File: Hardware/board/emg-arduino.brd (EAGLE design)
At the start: 27.9 x 50.5 mm, 23 parts, among them U1 ATMEGA328P_TQFP, U2 LIS3DH, U3 TC1262, U4 BLUEFRUIT-LE

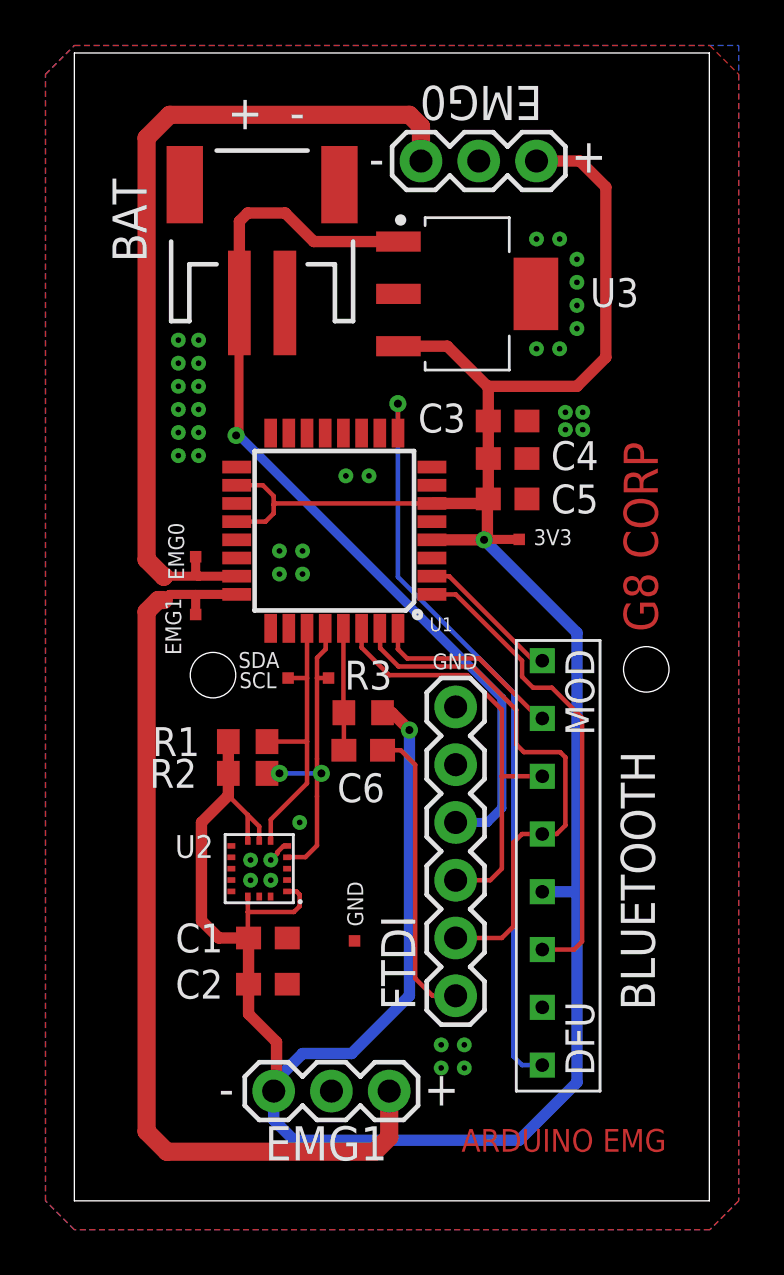
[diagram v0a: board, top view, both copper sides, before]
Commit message: changed bluetooth connector location
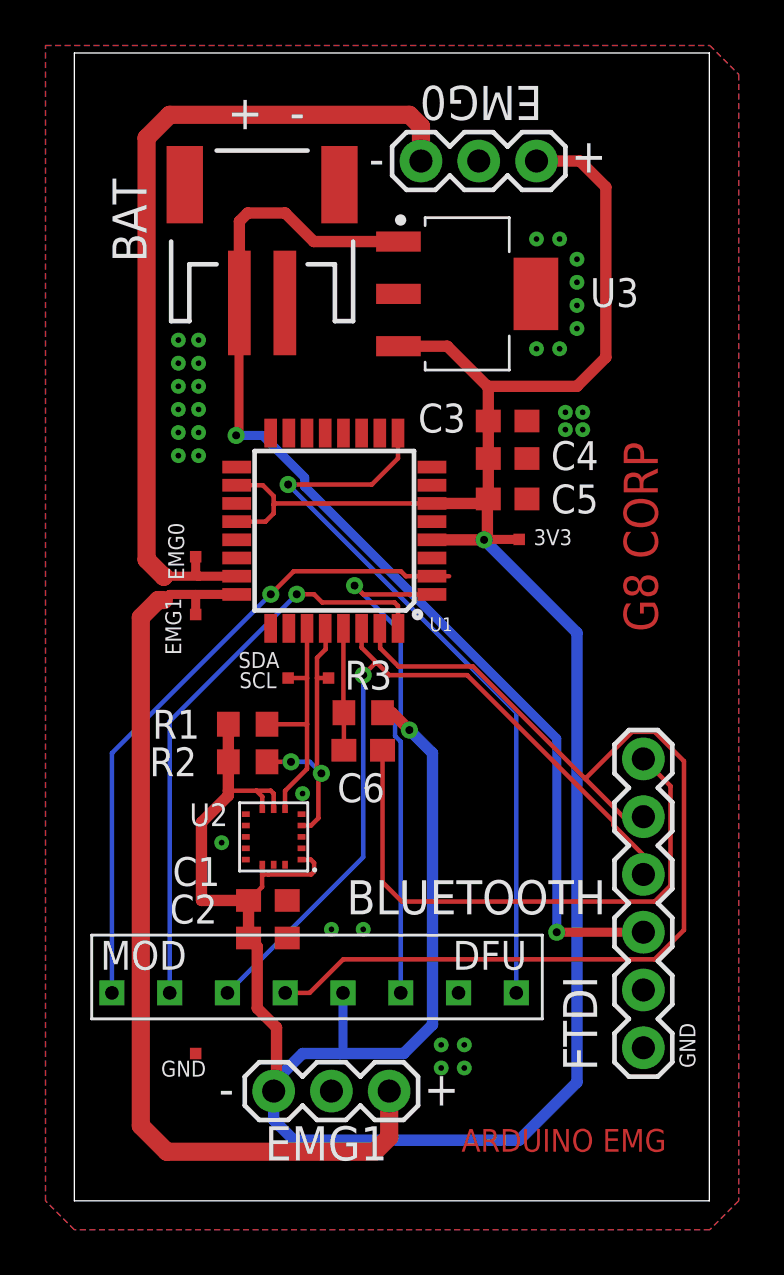
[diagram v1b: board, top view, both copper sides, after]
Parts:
- moved J1 13.3 mm to (25.0, 23.2), turned to 270 degrees
- moved U4 13.3 mm to (9.27, 13.0), turned to 0 degrees
- moved TP6 8.56 mm to (5.33, 10.3)
- moved C2 2.03 mm to (8.51, 15.4)
- moved C1 1.65 mm to (8.51, 17.0)
- moved U2 1.53 mm to (8.76, 19.8)
- moved R1 0.76 mm to (7.62, 24.8)
- moved R2 0.51 mm to (7.62, 23.1)
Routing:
- net AT_TXD: track 23.9 -> 47.4 mm
- net MOD: track 6.39 -> 28.8 mm, vias 0 -> 1
- net CTS: track 8.53 -> 25.8 mm, vias 0 -> 1
- net AT_RXD: track 19.1 -> 35.2 mm, vias 0 -> 1
- net N$6: track 13.2 -> 25.2 mm
- net VBAT: track 40.7 -> 49.3 mm, vias 1 -> 2
- net +3V3: track 137.2 -> 142.1 mm
- net SDA: track 12.6 -> 10.9 mm
- net SCL: track 14.4 -> 12.8 mm
- net RTS: track 21.5 -> 23.0 mm, vias 0 -> 1
- net GND: track 1.01 -> 0.00 mm, vias 39 -> 32
- net DFU: track 33.5 -> 32.9 mm

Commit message: it told to commit
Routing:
- net +3V3: track 142.1 -> 143.4 mm
- net MOD: track 28.8 -> 28.0 mm
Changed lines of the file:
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@@
 </layers>
 <board>
-<fusionsync huburn="a.cGVyc29uYWw6dWUyOTBkMjM5" projecturn="a.cGVyc29uYWw6dWUyOTBkMjM5IzIwMTkwMjE5MTc3MzQ1NTgx" f3durn="urn:adsk.wipprod:dm.lineage:8fWTQTV5RmWIqd0VZAsiqQ" pcbguid="3a42ec26-3a26-46cd-8abf-fc278c596440" lastpulledtime="" lastsyncedchangeguid="de925970-1e48-cc5d-e54b-a0e0153084cc"/>
+<fusionsync huburn="a.cGVyc29uYWw6dWUyOTBkMjM5" projecturn="a.cGVyc29uYWw6dWUyOTBkMjM5IzIwMTkwMjE5MTc3MzQ1NTgx" f3durn="urn:adsk.wipprod:dm.lineage:8fWTQTV5RmWIqd0VZAsiqQ" pcbguid="3a42ec26-3a26-46cd-8abf-fc278c596440" lastpulledtime="" lastsyncedchangeguid="fc1a16e9-a3e4-5bed-3485-182ead62ae13"/>
 <plain>
 <wire x1="0" y1="3.81" x2="27.92" y2="3.81" width="0" layer="20"/>
@@
 <text x="20.193" y="32.639" size="0.7" layer="25">3V3</text>
 <text x="3.81" y="9.271" size="0.7" layer="25">GND</text>
+<hole x="25.019" y="51.308" drill="2"/>
+<hole x="20.574" y="28.194" drill="2"/>
 </plain>
 <attributes>
@@
 <wire x1="18.161" y1="33.02" x2="18.161" y2="34.632" width="0.5" layer="1"/>
 <wire x1="18.161" y1="34.632" x2="18.2" y2="34.671" width="0.5" layer="1"/>
-<wire x1="22.098" y1="9.017" x2="22.098" y2="28.791" width="0.5" layer="16"/>
-<wire x1="22.098" y1="28.791" x2="18.015" y2="32.874" width="0.5" layer="16"/>
+<wire x1="22.86" y1="9.779" x2="22.86" y2="29.21" width="0.5" layer="16"/>
+<wire x1="22.86" y1="29.21" x2="19.196" y2="32.874" width="0.5" layer="16"/>
+<wire x1="19.196" y1="32.874" x2="18.015" y2="32.874" width="0.5" layer="16"/>
 <via x="18.015" y="32.874" extent="1-16" drill="0.35"/>
 <wire x1="7.659" y1="17.018" x2="7.659" y2="16.541" width="0.2" layer="1"/>
@@
 <wire x1="18.034" y1="32.893" x2="18.015" y2="32.874" width="0.4" layer="1"/>
 <wire x1="7.659" y1="15.367" x2="7.659" y2="17.018" width="0.5" layer="1"/>
-<wire x1="22.098" y1="9.017" x2="19.558" y2="6.477" width="0.5" layer="16"/>
+<wire x1="22.86" y1="9.779" x2="19.558" y2="6.477" width="0.5" layer="16"/>
 <wire x1="19.558" y1="6.477" x2="9.652" y2="6.477" width="0.5" layer="16"/>
 <wire x1="9.652" y1="6.477" x2="8.763" y2="7.366" width="0.5" layer="16"/>
@@
 <contactref element="U4" pad="MOD"/>
 <contactref element="U1" pad="2"/>
-<wire x1="16.478" y1="31.274" x2="15.7226" y2="31.274" width="0.2" layer="1"/>
 <wire x1="8.636" y1="30.48" x2="1.651" y2="23.495" width="0.2" layer="16"/>
 <wire x1="1.651" y1="12.954" x2="1.651" y2="23.495" width="0.2" layer="16"/>
